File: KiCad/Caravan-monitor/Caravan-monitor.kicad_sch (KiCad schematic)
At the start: 2 parts, among them IC2 STM32L011F4P6TR

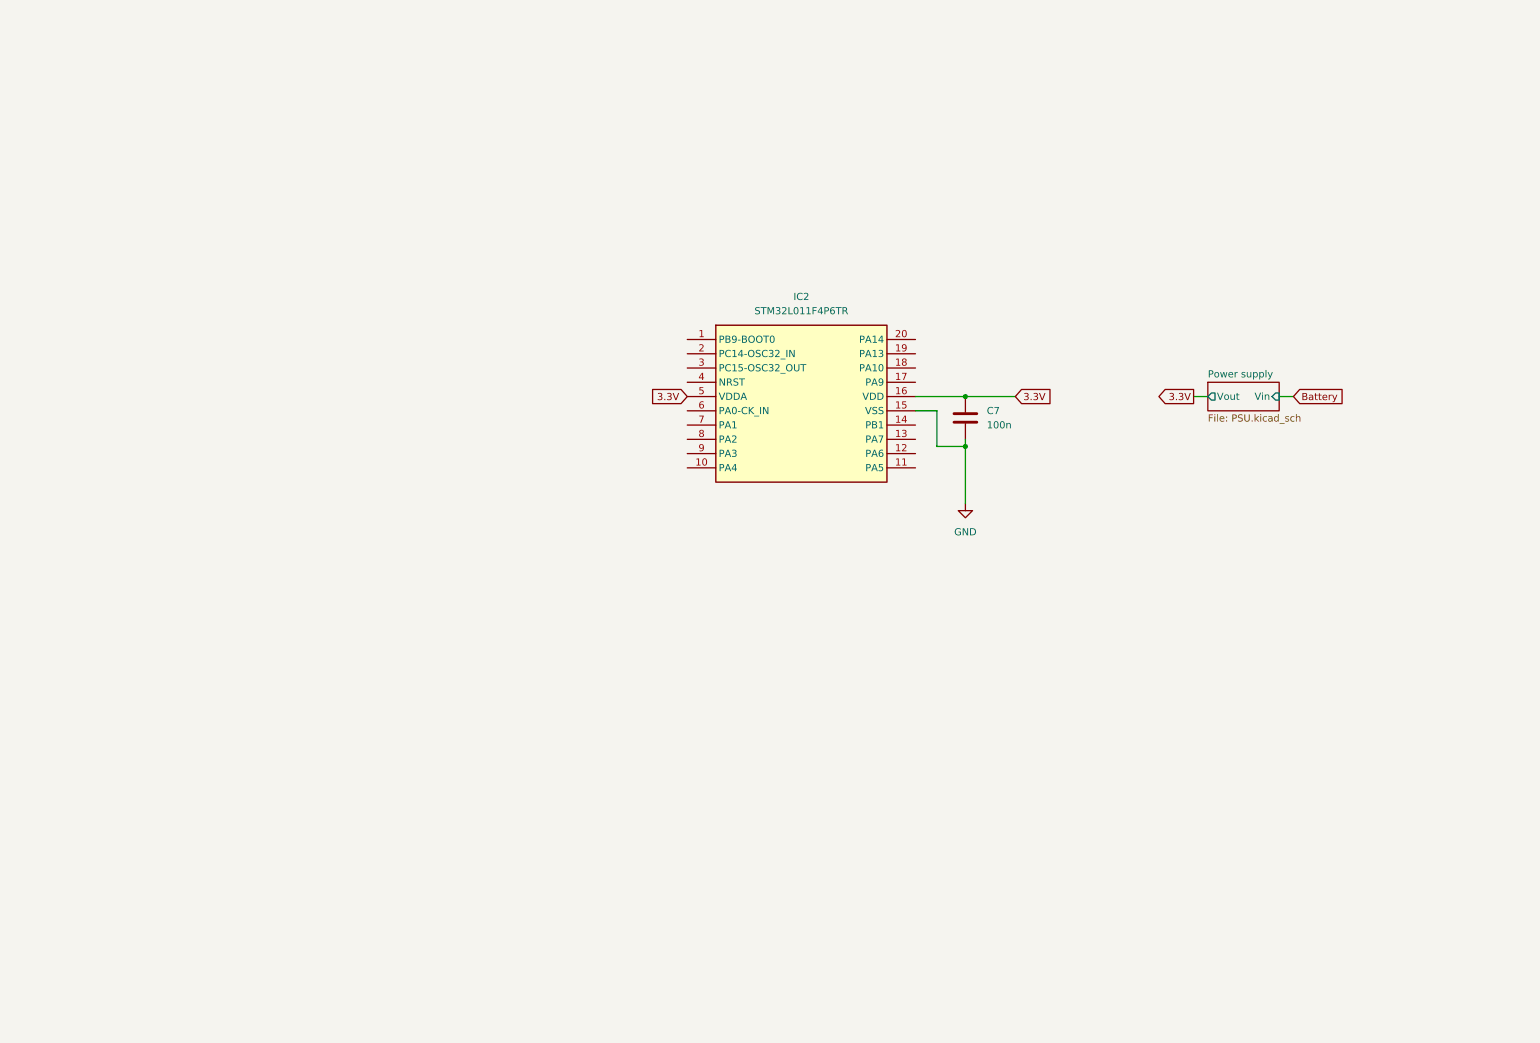
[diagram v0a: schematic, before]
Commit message: Battery voltage monitoring schematics
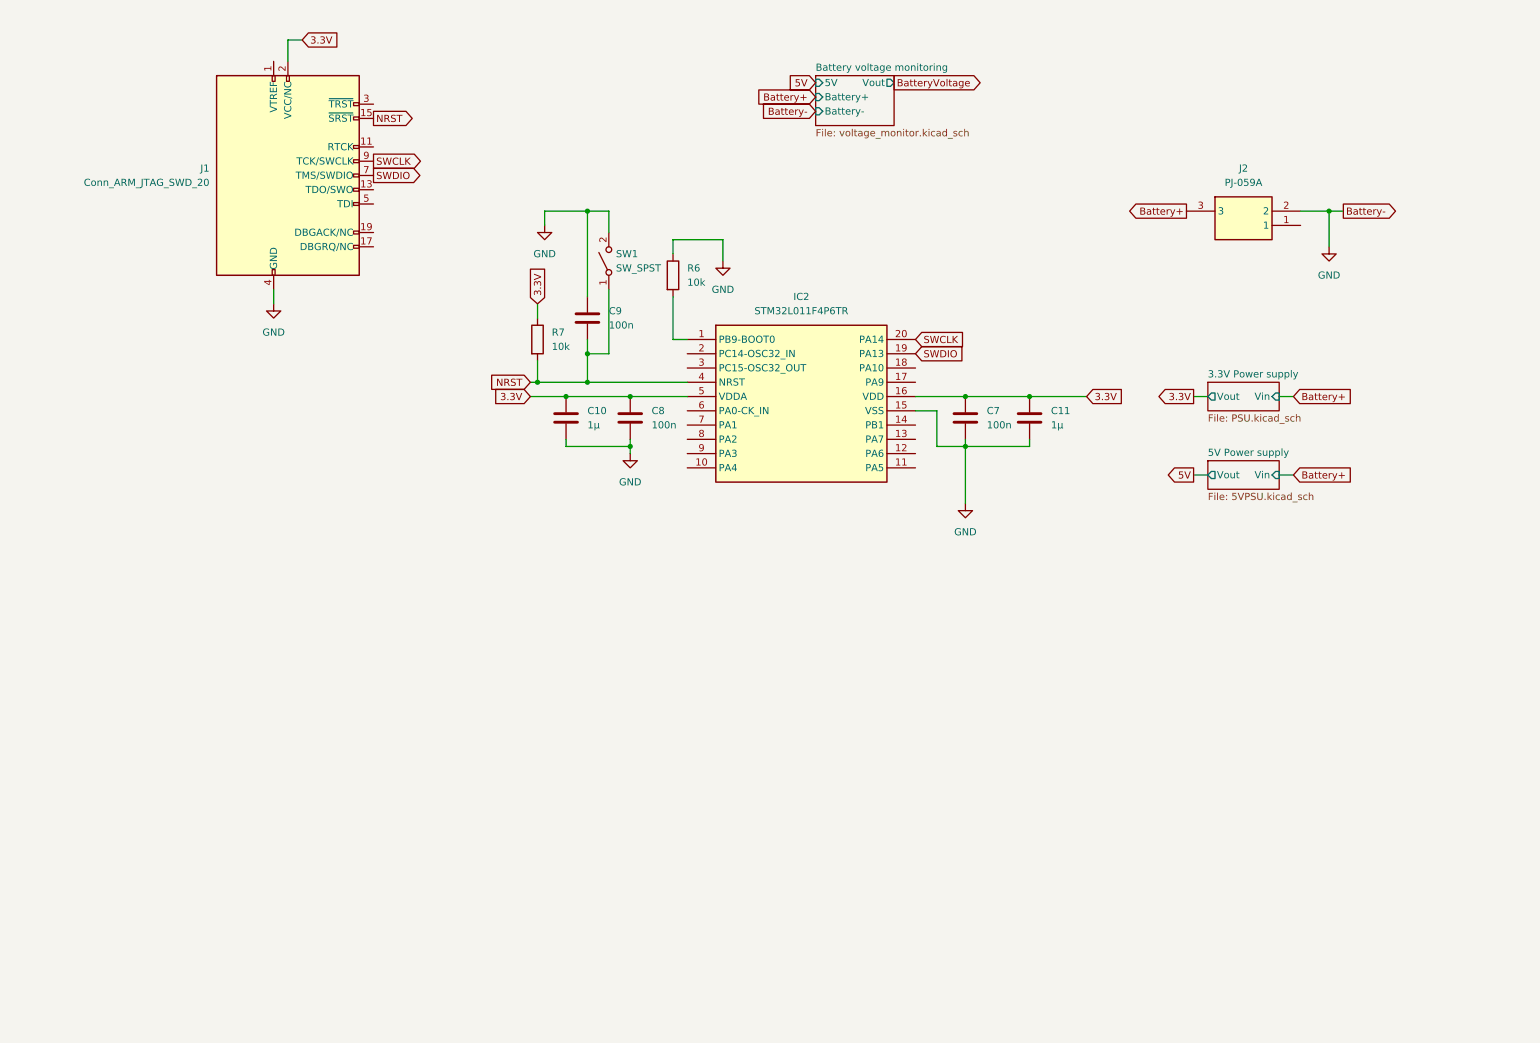
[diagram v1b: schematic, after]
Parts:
- added C10, C11: 1µ, Capacitor_SMD:C_0805_2012Metric_Pad1.18x1.45mm_HandSolder, symbol Device:C
- added C8, C9: 100n, Capacitor_SMD:C_0805_2012Metric_Pad1.18x1.45mm_HandSolder, symbol Device:C
- added J1: Conn_ARM_JTAG_SWD_20, Connector_IDC:IDC-Header_2x10_P2.54mm_Vertical, symbol Connector:Conn_ARM_JTAG_SWD_20
- added J2: PJ-059A, SamacSys_Parts:PJ059A, symbol SamacSys_Parts:PJ-059A
- added R6, R7: 10k, Resistor_SMD:R_0805_2012Metric_Pad1.20x1.40mm_HandSolder, symbol Device:R
- added SW1: SW_SPST, symbol Switch:SW_SPST
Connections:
- net 3.3V: now also C10.1, C11.1, C8.1, J1.2 (VCC/NC), R7.1
- net GND: now also C10.2, C11.2, C8.2, C9.1, J1.10 (GND), J1.12 (GND), J1.14 (GND), J1.16 (GND), J1.18 (GND), J1.20 (GND), J1.4 (GND), J1.6 (GND), J1.8 (GND), J2.2, R6.1, SW1.2 (B)
- net at IC2.1 (PB9-BOOT0): now also R6.2
- net SWDIO: now reaches IC2.19 (PA13)
- net SWDIO: now also J1.7 (TMS/SWDIO)
- net SWCLK: now reaches IC2.20 (PA14)
- net SWCLK: now also J1.9 (TCK/SWCLK)
- net NRST: now reaches IC2.4 (NRST)
- net NRST: now also C9.2, J1.15 (~{SRST}), R7.2, SW1.1 (A)
- new net Battery+: J2.3
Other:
- sheet Power supply renamed 3.3V Power supply
- added sheet 5V Power supply (5VPSU.kicad_sch)
- added sheet Battery voltage monitoring (voltage_monitor.kicad_sch)

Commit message: Temperature monitoring schematics
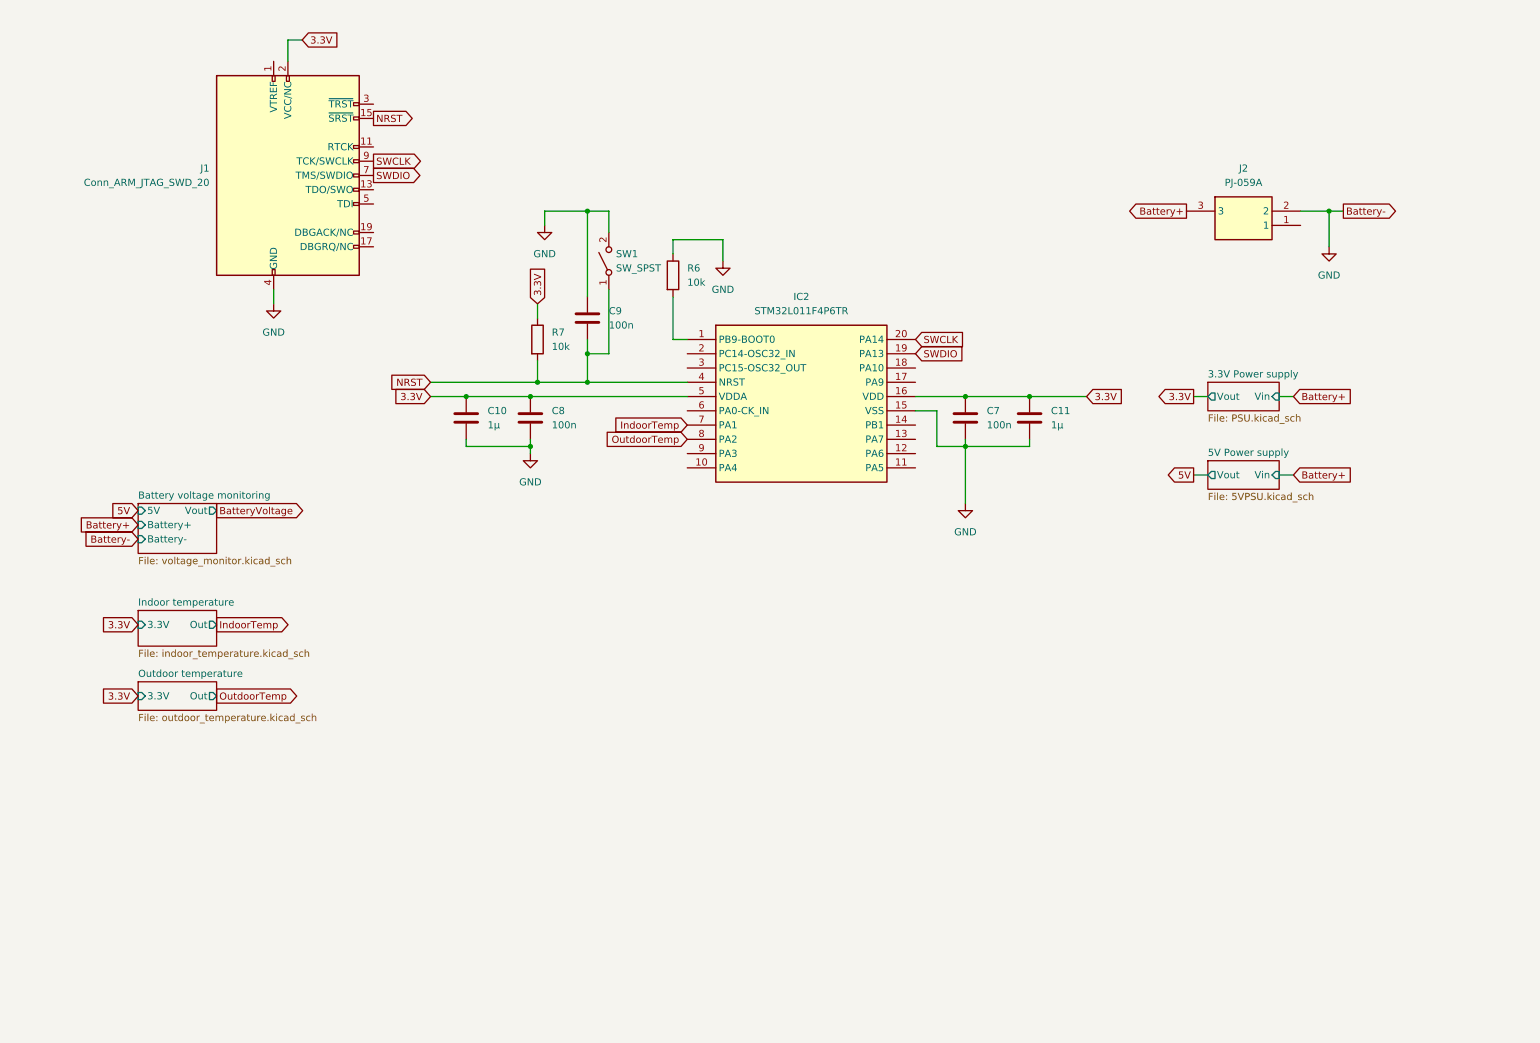
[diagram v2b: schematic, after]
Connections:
- net IndoorTemp: now reaches IC2.7 (PA1)
- net OutdoorTemp: now reaches IC2.8 (PA2)
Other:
- added sheet Indoor temperature (indoor_temperature.kicad_sch)
- added sheet Outdoor temperature (outdoor_temperature.kicad_sch)
- moved on the sheet: C10, C8

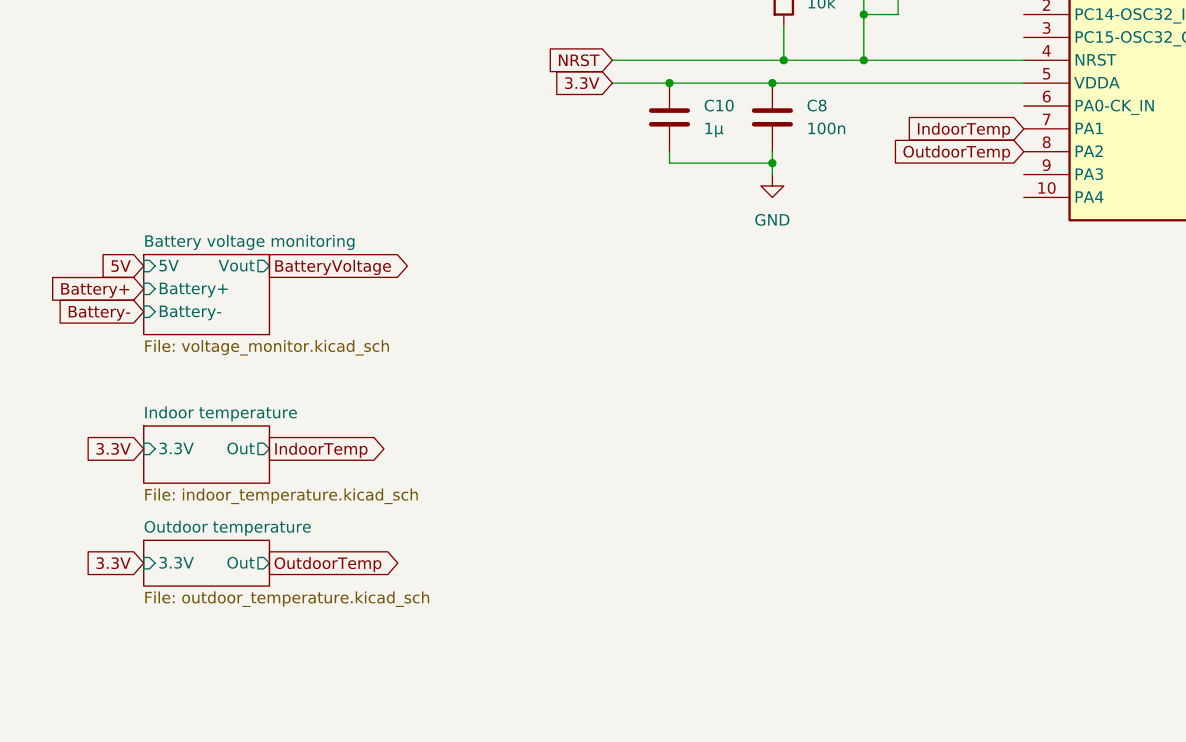
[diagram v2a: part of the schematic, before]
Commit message: Coolant temoerature measurement
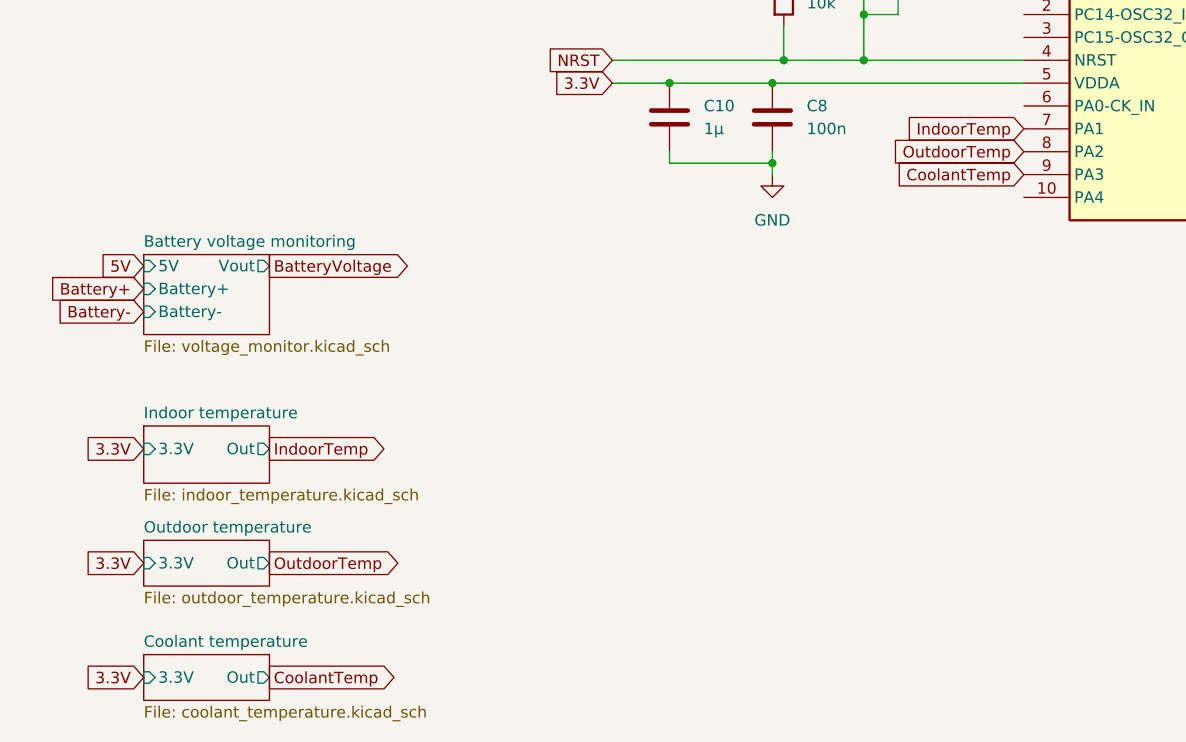
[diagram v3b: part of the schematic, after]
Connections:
- net CoolantTemp: now reaches IC2.9 (PA3)
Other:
- added sheet Coolant temperature (coolant_temperature.kicad_sch)
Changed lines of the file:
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@@
+		)
+	)
+	(global_label "CoolantTemp"
+		(shape input)
+		(at 132.08 93.98 180)
+		(fields_autoplaced yes)
+		(effects
+			(font
+				(size 1.27 1.27)
+			)
+			(justify right)
+		)
+		(property "Intersheetrefs" "${INTERSHEET_REFS}"
+			(at 116.9394 93.98 0)
+			(effects
+				(font
+					(size 1.27 1.27)
+				)
+				(justify right)
+				(hide yes)
+			)
 		)
 	)
@@
 		)
 	)
+	(global_label "3.3V"
+		(shape input)
+		(at 34.29 149.86 180)
+		(fields_autoplaced yes)
+		(effects
+			(font
+				(size 1.27 1.27)
+			)
+			(justify right)
+		)
+		(property "Intersheetrefs" "${INTERSHEET_REFS}"
+			(at 27.1924 149.86 0)
+			(effects
+				(font
+					(size 1.27 1.27)
+				)
+				(justify right)
+				(hide yes)
+			)
+		)
+	)
 	(global_label "SWDIO"
 		(shape output)
@@
 		(property "Intersheetrefs" "${INTERSHEET_REFS}"
 			(at 70.5976 20.32 0)
+			(effects
+				(font
+					(size 1.27 1.27)
+				)
+				(justify left)
+				(hide yes)
+			)
+		)
+	)
+	(global_label "CoolantTemp"
+		(shape output)
+		(at 48.26 149.86 0)
+		(fields_autoplaced yes)
+		(effects
+			(font
+				(size 1.27 1.27)
+			)
+			(justify left)
+		)
+		(property "Intersheetrefs" "${INTERSHEET_REFS}"
+			(at 63.4006 149.86 0)
 			(effects
 				(font
@@
 				)
 			)
+		)
+	)
+	(sheet
+		(at 34.29 147.32)
+		(size 13.97 5.08)
+		(exclude_from_sim no)
+		(in_bom yes)
+		(on_board yes)
+		(dnp no)
+		(fields_autoplaced yes)
+		(stroke
+			(width 0.1524)
+			(type solid)
+		)
+		(fill
+			(color 0 0 0 0.0000)
+		)
+		(property "Sheetname" "Coolant temperature"
+			(at 34.29 146.6084 0)
+			(effects
+				(font
+					(size 1.27 1.27)
+				)
+				(justify left bottom)
+			)
+		)
+		(property "Sheetfile" "coolant_temperature.kicad_sch"
+			(at 34.29 152.9846 0)
+			(effects
+				(font
+					(size 1.27 1.27)
+				)
+				(justify left top)
+			)
+		)
+		(pin "3.3V" input
+			(at 34.29 149.86 180)
+			(effects
+				(font
+					(size 1.27 1.27)
+				)
+				(justify left)
+			)
+		)
+		(pin "Out" output
+			(at 48.26 149.86 0)
+			(effects
+				(font
+					(size 1.27 1.27)
+				)
+				(justify right)
+			)
+		)
+		(instances
+			(project "Caravan-monitor"
+				(path "/4b94aa5f-1c73-4d2e-8117-e53a25103462"
+					(page "7")
+				)
+			)
